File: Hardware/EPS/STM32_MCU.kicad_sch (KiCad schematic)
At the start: 32 parts, among them J201 Conn_ARM_JTAG_SWD_10, U201 STM32L431RCT, U202 HZ0805E601R-10

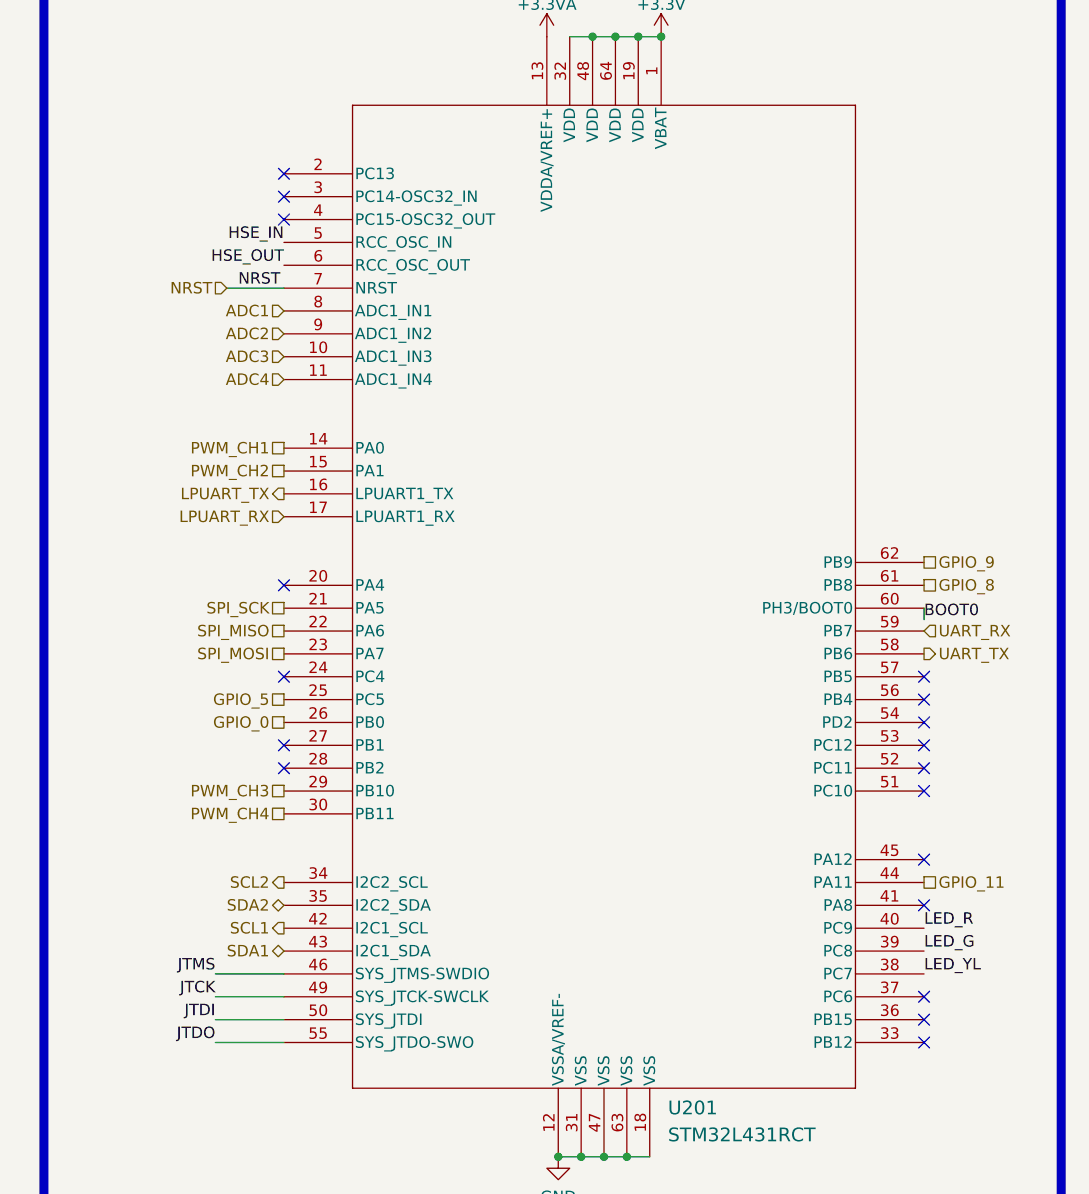
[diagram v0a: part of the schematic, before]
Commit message: Changed uC pinout and finished uC routing
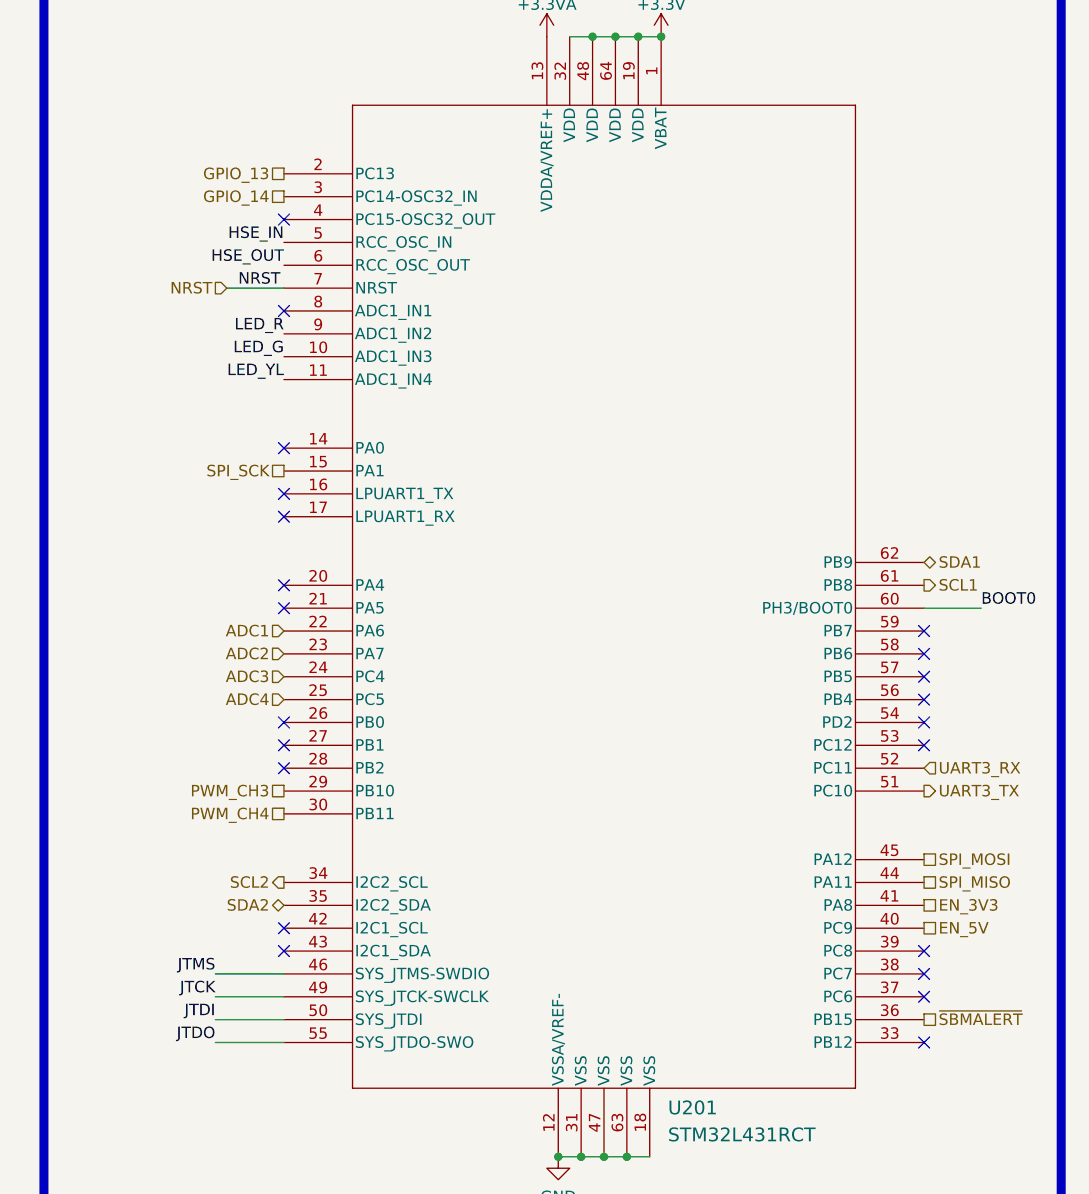
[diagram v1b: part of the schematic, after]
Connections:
- net GPIO_11 is gone; now on net SPI_MISO: U201.44 (PA11)
- net GPIO_5 is gone; now on net ADC4: U201.25 (PC5)
- net GPIO_8 is gone; now on net SCL1: U201.61 (PB8)
- net GPIO_9 is gone; now on net SDA1: U201.62 (PB9)
- net PWM_CH2 is gone; now on net SPI_SCK: U201.15 (PA1)
- net ADC1: now also U201.22 (PA6); no longer U201.8 (ADC1_IN1)
- net ADC2: now also U201.23 (PA7); no longer U201.9 (ADC1_IN2)
- net ADC3: now also U201.24 (PC4); no longer U201.10 (ADC1_IN3)
- net ADC4: no longer U201.11 (ADC1_IN4)
- net LED_G: now also U201.10 (ADC1_IN3); no longer U201.39 (PC8)
- net LED_R: now also U201.9 (ADC1_IN2); no longer U201.40 (PC9)
- net LED_YL: now also U201.11 (ADC1_IN4); no longer U201.38 (PC7)
- net SCL1: no longer U201.42 (I2C1_SCL)
- net SDA1: no longer U201.43 (I2C1_SDA)
- net SPI_MISO: no longer U201.22 (PA6)
- net SPI_MOSI: now also U201.45 (PA12); no longer U201.23 (PA7)
- net SPI_SCK: no longer U201.21 (PA5)
- net GPIO_13: now reaches U201.2 (PC13)
- net GPIO_14: now reaches U201.3 (PC14-OSC32_IN)
- net ~{SBMALERT}: now reaches U201.36 (PB15)
- net EN_3V3: now reaches U201.41 (PA8)
- net UART3_TX: now reaches U201.51 (PC10)
- net UART3_RX: now reaches U201.52 (PC11)
- net GPIO_0: no longer names the net of U201.26 (PB0)
- net LPUART_RX: no longer names the net of U201.17 (LPUART1_RX)
- net LPUART_TX: no longer names the net of U201.16 (LPUART1_TX)
- net PWM_CH1: no longer names the net of U201.14 (PA0)
- net UART_RX: no longer names the net of U201.59 (PB7)
- net UART_TX: no longer names the net of U201.58 (PB6)
- new net EN_5V: U201.40 (PC9)
- no-connect marks 18 -> 22
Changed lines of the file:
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@@
   (junction (at 101.6 166.37) (diameter 0) (color 0 0 0 0)
   )
-  (no_connect (at 264.16 107.95))
-  (no_connect (at 264.16 110.49))
+  (no_connect (at 193.04 59.69))
+  (no_connect (at 264.16 130.81))
   (no_connect (at 193.04 49.53))
-  (no_connect (at 264.16 125.73))
   (no_connect (at 264.16 102.87))
-  (no_connect (at 193.04 44.45))
+  (no_connect (at 193.04 105.41))
+  (no_connect (at 193.04 128.27))
+  (no_connect (at 193.04 82.55))
+  (no_connect (at 193.04 80.01))
   (no_connect (at 193.04 107.95))
-  (no_connect (at 193.04 46.99))
-  (no_connect (at 193.04 100.33))
-  (no_connect (at 264.16 113.03))
+  (no_connect (at 193.04 92.71))
   (no_connect (at 193.04 90.17))
-  (no_connect (at 264.16 138.43))
+  (no_connect (at 193.04 74.93))
+  (no_connect (at 264.16 97.79))
+  (no_connect (at 193.04 130.81))
   (no_connect (at 264.16 105.41))
   (no_connect (at 264.16 135.89))
   (no_connect (at 264.16 100.33))
   (no_connect (at 264.16 140.97))
-  (no_connect (at 264.16 120.65))
+  (no_connect (at 264.16 95.25))
   (no_connect (at 193.04 110.49))
+  (no_connect (at 264.16 107.95))
+  (no_connect (at 264.16 133.35))
   (wire (pts (xy 129.54 62.23) (xy 129.54 68.58))
     (stroke (width 0) (type default) (color 0 0 0 0))
@@
     (stroke (width 0) (type default) (color 0 0 0 0))
   )
-  (wire (pts (xy 264.16 93.98) (xy 264.16 92.71))
+  (wire (pts (xy 270.51 92.71) (xy 264.16 92.71))
     (stroke (width 0) (type default) (color 0 0 0 0))
   )
@@
     (effects (font (size 1.27 1.27)) (justify left bottom))
   )
+  (label "LED_G" (at 193.04 64.77 180)
+    (effects (font (size 1.27 1.27)) (justify right bottom))
+  )
   (label "JTCK" (at 69.85 165.1 0)
     (effects (font (size 1.27 1.27)) (justify left bottom))
@@
     (effects (font (size 1.27 1.27)) (justify left bottom))
   )
-  (label "LED_G" (at 264.16 130.81 0)
-    (effects (font (size 1.27 1.27)) (justify left bottom))
-  )
   (label "JTMS" (at 185.42 133.35 180)
     (effects (font (size 1.27 1.27)) (justify right bottom))
@@
     (effects (font (size 1.27 1.27)) (justify left bottom))
   )
-  (label "BOOT0" (at 264.16 93.98 0)
+  (label "BOOT0" (at 270.51 92.71 0)
     (effects (font (size 1.27 1.27)) (justify left bottom))
+  )
+  (label "LED_YL" (at 193.04 67.31 180)
+    (effects (font (size 1.27 1.27)) (justify right bottom))
   )
   (label "HSE_IN" (at 193.04 52.07 180)
     (effects (font (size 1.27 1.27)) (justify right bottom))
   )
-  (label "LED_YL" (at 264.16 133.35 0)
-    (effects (font (size 1.27 1.27)) (justify left bottom))
-  )
   (label "JTCK" (at 185.42 135.89 180)
     (effects (font (size 1.27 1.27)) (justify right bottom))
@@
     (effects (font (size 1.27 1.27)) (justify left bottom))
   )
+  (label "LED_R" (at 193.04 62.23 180)
+    (effects (font (size 1.27 1.27)) (justify right bottom))
+  )
   (label "NRST" (at 143.51 105.41 0)
     (effects (font (size 1.27 1.27)) (justify left bottom))
   )
-  (label "LED_R" (at 264.16 128.27 0)
-    (effects (font (size 1.27 1.27)) (justify left bottom))
-  )
   (label "NRST" (at 187.96 57.15 0)
     (effects (font (size 1.27 1.27)) (justify left bottom))
@@
     (effects (font (size 1.27 1.27)) (justify left bottom))
   )
-  (hierarchical_label "GPIO_8" (shape passive) (at 264.16 90.17 0)
-    (effects (font (size 1.27 1.27)) (justify left))
-  )
   (hierarchical_label "SCL1" (shape output) (at 129.54 68.58 0)
     (effects (font (size 1.27 1.27)) (justify left))
   )
-  (hierarchical_label "PWM_CH1" (shape passive) (at 193.04 74.93 180)
+  (hierarchical_label "SPI_SCK" (shape passive) (at 193.04 77.47 180)
     (effects (font (size 1.27 1.27)) (justify right))
   )
-  (hierarchical_label "SPI_MISO" (shape passive) (at 193.04 95.25 180)
+  (hierarchical_label "ADC4" (shape input) (at 193.04 102.87 180)
     (effects (font (size 1.27 1.27)) (justify right))
   )
-  (hierarchical_label "UART_RX" (shape input) (at 264.16 95.25 0)
+  (hierarchical_label "ADC2" (shape input) (at 193.04 97.79 180)
+    (effects (font (size 1.27 1.27)) (justify right))
+  )
+  (hierarchical_label "SDA1" (shape bidirectional) (at 264.16 87.63 0)
     (effects (font (size 1.27 1.27)) (justify left))
-  )
-  (hierarchical_label "ADC4" (shape input) (at 193.04 67.31 180)
-    (effects (font (size 1.27 1.27)) (justify right))
   )
   (hierarchical_label "PWM_CH3" (shape passive) (at 193.04 113.03 180)
     (effects (font (size 1.27 1.27)) (justify right))
   )
-  (hierarchical_label "SPI_MOSI" (shape passive) (at 193.04 97.79 180)
-    (effects (font (size 1.27 1.27)) (justify right))
-  )
   (hierarchical_label "SCL2" (shape output) (at 193.04 123.19 180)
     (effects (font (size 1.27 1.27)) (justify right))
   )
-  (hierarchical_label "ADC2" (shape input) (at 193.04 62.23 180)
-    (effects (font (size 1.27 1.27)) (justify right))
-  )
-  (hierarchical_label "ADC1" (shape input) (at 193.04 59.69 180)
-    (effects (font (size 1.27 1.27)) (justify right))
-  )
-  (hierarchical_label "GPIO_9" (shape passive) (at 264.16 87.63 0)
+  (hierarchical_label "UART3_RX" (shape input) (at 264.16 110.49 0)
+    (effects (font (size 1.27 1.27)) (justify left))
+  )
+  (hierarchical_label "EN_3V3" (shape passive) (at 264.16 125.73 0)
     (effects (font (size 1.27 1.27)) (justify left))
   )
@@
     (effects (font (size 1.27 1.27)) (justify right))
   )
-  (hierarchical_label "GPIO_0" (shape passive) (at 193.04 105.41 180)
-    (effects (font (size 1.27 1.27)) (justify right))
-  )
-  (hierarchical_label "SCL1" (shape output) (at 193.04 128.27 180)
-    (effects (font (size 1.27 1.27)) (justify right))
-  )
-  (hierarchical_label "LPUART_TX" (shape output) (at 193.04 80.01 180)
-    (effects (font (size 1.27 1.27)) (justify right))
-  )
-  (hierarchical_label "UART_TX" (shape output) (at 264.16 97.79 0)
+  (hierarchical_label "~{SBMALERT}" (shape passive) (at 264.16 138.43 0)
+    (effects (font (size 1.27 1.27)) (justify left))
+  )
+  (hierarchical_label "SCL1" (shape output) (at 264.16 90.17 0)
+    (effects (font (size 1.27 1.27)) (justify left))
+  )
+  (hierarchical_label "UART3_TX" (shape output) (at 264.16 113.03 0)
     (effects (font (size 1.27 1.27)) (justify left))
   )
@@
     (effects (font (size 1.27 1.27)) (justify left))
   )
-  (hierarchical_label "LPUART_RX" (shape input) (at 193.04 82.55 180)
+  (hierarchical_label "SPI_MISO" (shape passive) (at 264.16 123.19 0)
+    (effects (font (size 1.27 1.27)) (justify left))
+  )
+  (hierarchical_label "SPI_MOSI" (shape passive) (at 264.16 120.65 0)
+    (effects (font (size 1.27 1.27)) (justify left))
+  )
+  (hierarchical_label "EN_5V" (shape passive) (at 264.16 128.27 0)
+    (effects (font (size 1.27 1.27)) (justify left))
+  )
+  (hierarchical_label "ADC3" (shape input) (at 193.04 100.33 180)
     (effects (font (size 1.27 1.27)) (justify right))
   )
-  (hierarchical_label "SDA1" (shape bidirectional) (at 193.04 130.81 180)
+  (hierarchical_label "GPIO_14" (shape passive) (at 193.04 46.99 180)
     (effects (font (size 1.27 1.27)) (justify right))
   )
@@
     (effects (font (size 1.27 1.27)) (justify right))
   )
-  (hierarchical_label "GPIO_11" (shape passive) (at 264.16 123.19 0)
-    (effects (font (size 1.27 1.27)) (justify left))
+  (hierarchical_label "ADC1" (shape input) (at 193.04 95.25 180)
+    (effects (font (size 1.27 1.27)) (justify right))
   )
   (hierarchical_label "SDA1" (shape bidirectional) (at 137.16 68.58 0)
     (effects (font (size 1.27 1.27)) (justify left))
   )
-  (hierarchical_label "SPI_SCK" (shape passive) (at 193.04 92.71 180)
+  (hierarchical_label "GPIO_13" (shape passive) (at 193.04 44.45 180)
     (effects (font (size 1.27 1.27)) (justify right))
   )
-  (hierarchical_label "ADC3" (shape input) (at 193.04 64.77 180)
-    (effects (font (size 1.27 1.27)) (justify right))
-  )
-  (hierarchical_label "GPIO_5" (shape passive) (at 193.04 102.87 180)
-    (effects (font (size 1.27 1.27)) (justify right))
-  )
-  (hierarchical_label "PWM_CH2" (shape passive) (at 193.04 77.47 180)
-    (effects (font (size 1.27 1.27)) (justify right))
-  )

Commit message: Finished EPS - v0.1.0
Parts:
- C209: value 0.1uF -> 100nF
- U201: footprint STM32L431RCT6:QFP50P1200X1200X160-64N -> STM32L431RCT:LQFP-64
- XTAL201: footprint NX5032GA-8.000M:XTAL_NX5032_NDK-M -> NX5032GA-8.000M:XTAL_NX5032_NDK
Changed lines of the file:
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@@
   (title_block
     (title "EPS Schematics")
-    (date "2023-04-08")
-    (rev "v0.0.3")
-    (comment 1 "e-mail: ")
+    (date "2023-04-19")
+    (rev "v0.1.0")
+    (comment 1 "LinkedIn: linkedin.com/in/carlos-martinez-mora-7b2023230/")
     (comment 2 "Author: Carlos Martinez Mora")
   )
@@
       (effects (font (size 1.524 1.524)) (justify left))
     )
-    (property "Footprint" "STM32L431RCT6:QFP50P1200X1200X160-64N" (id 2) (at 193.04 41.91 0)
+    (property "Footprint" "STM32L431RCT:LQFP-64" (id 2) (at 193.04 41.91 0)
       (effects (font (size 1.27 1.27) italic) hide)
     )
@@
       (effects (font (size 1.27 1.27)) (justify left))
     )
-    (property "Value" "0.1uF" (id 1) (at 146.431 111.5572 0)
+    (property "Value" "100nF" (id 1) (at 146.431 111.5572 0)
       (effects (font (size 1.27 1.27)) (justify left))
     )
@@
       (effects (font (size 1.524 1.524)))
     )
-    (property "Footprint" "NX5032GA-8.000M:XTAL_NX5032_NDK-M" (id 2) (at 106.68 157.226 0)
+    (property "Footprint" "NX5032GA-8.000M:XTAL_NX5032_NDK" (id 2) (at 106.68 157.226 0)
       (effects (font (size 1.524 1.524)) hide)
     )
